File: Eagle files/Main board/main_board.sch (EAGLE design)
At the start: 63 parts, among them X1 ARK2, X2 ARK1

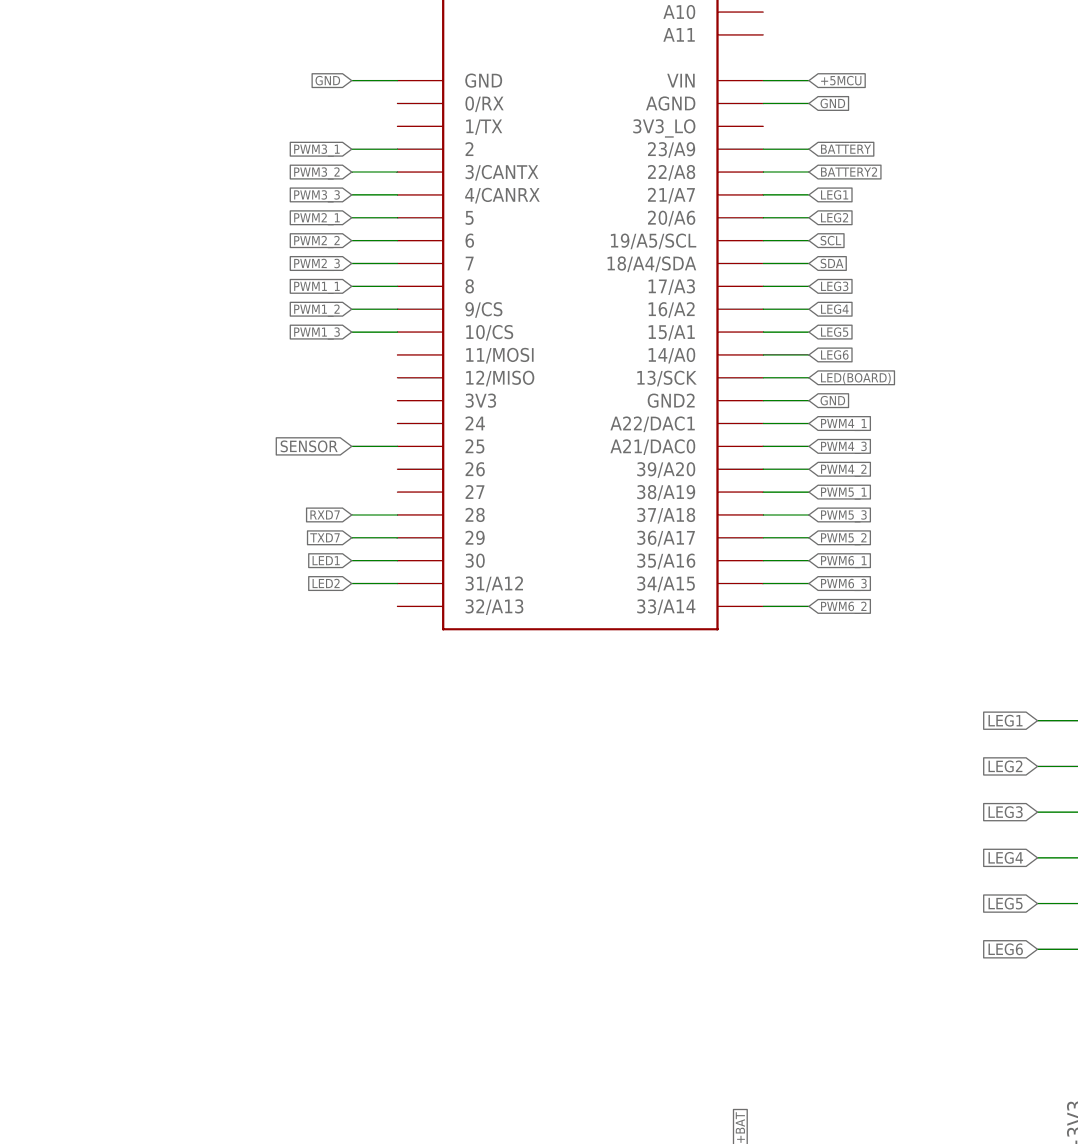
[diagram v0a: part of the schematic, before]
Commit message: update pcb
-increase servo power line width
-added step-down regulator enable
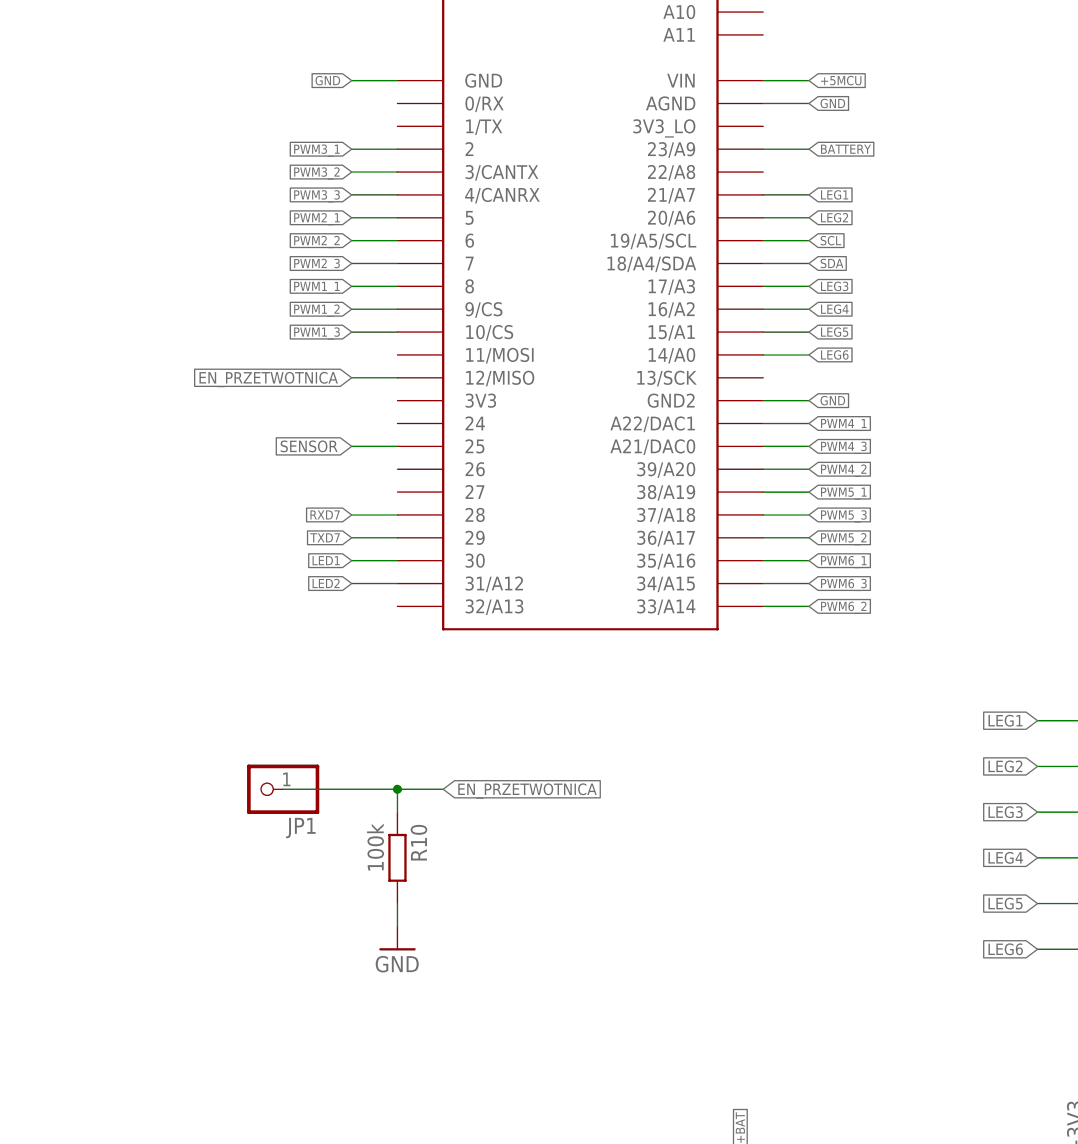
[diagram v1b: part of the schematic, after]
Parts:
- added JP1: (no value), pinhead:PINHD-1X1
- added R10: 100k, rcl:R-EU_R0805
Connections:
- removed net BATTERY2: TEENSY41.22/A8
- removed net LED(BOARD): TEENSY41.13/SCK
- new net EN_PRZETWOTNICA: JP1.1, R10.1, TEENSY41.12/MISO
- net GND: now also R10.2
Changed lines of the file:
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@@
 <part name="C19" library="rcl" deviceset="C-EU" device="C0805" value="100n"/>
 <part name="C20" library="rcl" deviceset="C-EU" device="C1206" value="10uF"/>
+<part name="JP1" library="pinhead" deviceset="PINHD-1X1" device=""/>
+<part name="R10" library="rcl" deviceset="R-EU_" device="R0805" value="100k"/>
+<part name="GND6" library="supply1" deviceset="GND" device=""/>
 </parts>
 <sheets>
@@
 <instance part="C19" gate="G$1" x="152.4" y="137.16"/>
 <instance part="C20" gate="G$1" x="162.56" y="137.16"/>
+<instance part="JP1" gate="G$1" x="0" y="73.66" rot="R180"/>
+<instance part="R10" gate="G$1" x="15.24" y="66.04" rot="R270"/>
+<instance part="GND6" gate="1" x="15.24" y="55.88"/>
 </instances>
 <busses>
@@
 <pinref part="GND2" gate="1" pin="GND"/>
 </segment>
+<segment>
+<pinref part="GND6" gate="1" pin="GND"/>
+<pinref part="R10" gate="G$1" pin="2"/>
+<wire x1="15.24" y1="58.42" x2="15.24" y2="60.96" width="0.1524" layer="91"/>
+</segment>
 </net>
 <net name="PWM1_1" class="0">
@@
 </segment>
 </net>
-<net name="LED(BOARD)" class="0">
-<segment>
-<pinref part="TEENSY41" gate="G$1" pin="13/SCK"/>
-<wire x1="55.88" y1="119.38" x2="60.96" y2="119.38" width="0.1524" layer="91"/>
-<label x="60.96" y="119.38" size="1.016" layer="95" xref="yes"/>
-</segment>
-</net>
 <net name="N$1" class="0">
 <segment>
@@
 <label x="81.28" y="243.84" size="1.016" layer="95" rot="R180" xref="yes"/>
 <pinref part="BATERIA" gate="-1" pin="KL"/>
-</segment>
-</net>
-<net name="BATTERY2" class="0">
-<segment>
-<pinref part="TEENSY41" gate="G$1" pin="22/A8"/>
-<wire x1="55.88" y1="142.24" x2="60.96" y2="142.24" width="0.1524" layer="91"/>
-<label x="60.96" y="142.24" size="1.016" layer="95" xref="yes"/>
 </segment>
 </net>
@@
 </segment>
 </net>
+<net name="EN_PRZETWOTNICA" class="0">
+<segment>
+<pinref part="TEENSY41" gate="G$1" pin="12/MISO"/>
+<wire x1="15.24" y1="119.38" x2="10.16" y2="119.38" width="0.1524" layer="91"/>
+<label x="10.16" y="119.38" size="1.27" layer="95" rot="R180" xref="yes"/>
+</segment>
+<segment>
+<wire x1="2.54" y1="73.66" x2="15.24" y2="73.66" width="0.1524" layer="91"/>
+<label x="20.32" y="73.66" size="1.27" layer="95" xref="yes"/>
+<pinref part="JP1" gate="G$1" pin="1"/>
+<pinref part="R10" gate="G$1" pin="1"/>
+<wire x1="15.24" y1="73.66" x2="20.32" y2="73.66" width="0.1524" layer="91"/>
+<wire x1="15.24" y1="71.12" x2="15.24" y2="73.66" width="0.1524" layer="91"/>
+<junction x="15.24" y="73.66"/>
+</segment>
+</net>
